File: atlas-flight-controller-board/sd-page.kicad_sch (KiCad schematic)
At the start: 1 part, among them J1 Conn_01x07_Socket

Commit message: finishing up schematic for v1.
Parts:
- J3: renamed from J1; value Conn_01x07_Socket -> XTSD Socket
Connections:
- net +3V3: now reaches J3.2 (Pin_2)
- net GND: now reaches J3.3 (Pin_3)
- net SCK: now reaches J3.4 (Pin_4)
- net MISO: now reaches J3.5 (Pin_5)
- net MOSI: now reaches J3.6 (Pin_6)
- net SD_CS: now reaches J3.7 (Pin_7)
- no-connect marks 0 -> 1

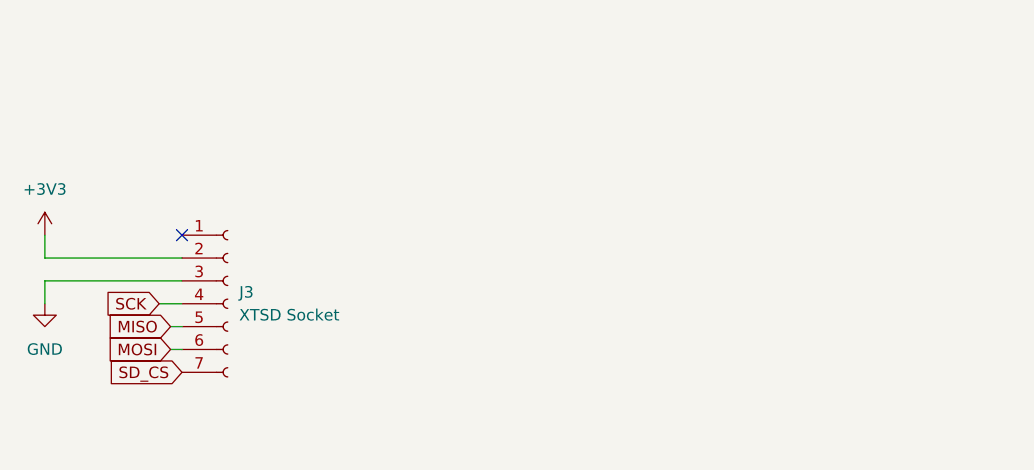
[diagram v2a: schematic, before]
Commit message: removing some olds symbols, adding some new things such as nand flash chip.
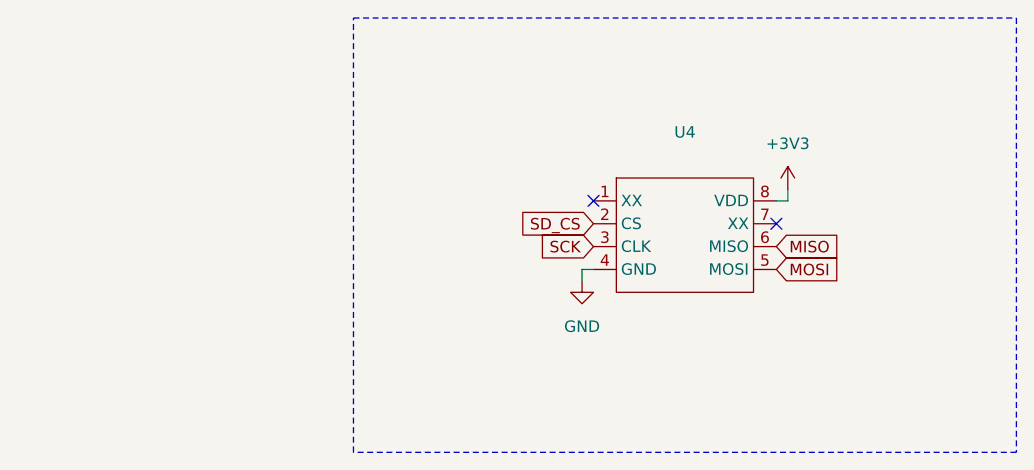
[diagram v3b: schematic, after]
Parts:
- removed J3: XTSD Socket, Connector_PinSocket_2.54mm:PinSocket_1x07_P2.54mm_Vertical, symbol Connector:Conn_01x07_Socket
- added U4: ~, ZDSD16GLGIAG:LGA-8_8x6.2mm_P1.27mm, symbol Interface:ZDSD16GLGIAG
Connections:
- net +3V3: now also U4.8 (VDD)
- net GND: now also U4.4 (GND)
- net MISO: now also U4.6 (MISO)
- net MOSI: now also U4.5 (MOSI)
- net SCK: now also U4.3 (CLK)
- net SD_CS: now also U4.2 (CS)
- no-connect marks 1 -> 2
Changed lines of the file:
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@@
 	(generator_version "9.0")
 	(paper "A4")
+	(rectangle
+		(start 149.86 59.69)
+		(end 223.52 107.95)
+		(stroke
+			(width 0)
+			(type dash)
+		)
+		(fill
+			(type none)
+		)
+	)
 	(no_connect
-		(at 130.81 83.82)
+		(at 196.85 82.55)
+	)
+	(no_connect
+		(at 176.53 80.01)
 	)
 	(wire
 		(pts
-			(xy 115.57 88.9) (xy 115.57 91.44)
+			(xy 175.26 88.9) (xy 175.26 87.63)
 		)
 		(stroke
@@
 	(wire
 		(pts
-			(xy 129.54 96.52) (xy 130.81 96.52)
+			(xy 175.26 87.63) (xy 176.53 87.63)
 		)
 		(stroke
@@
 	(wire
 		(pts
-			(xy 128.27 91.44) (xy 130.81 91.44)
+			(xy 196.85 80.01) (xy 198.12 80.01)
 		)
 		(stroke
@@
 	(wire
 		(pts
-			(xy 129.54 93.98) (xy 130.81 93.98)
-		)
-		(stroke
-			(width 0)
-			(type default)
-		)
-	)
-	(wire
-		(pts
-			(xy 115.57 86.36) (xy 115.57 83.82)
-		)
-		(stroke
-			(width 0)
-			(type default)
-		)
-	)
-	(wire
-		(pts
-			(xy 130.81 86.36) (xy 115.57 86.36)
-		)
-		(stroke
-			(width 0)
-			(type default)
-		)
-	)
-	(wire
-		(pts
-			(xy 130.81 88.9) (xy 115.57 88.9)
+			(xy 198.12 80.01) (xy 198.12 78.74)
 		)
 		(stroke
@@
 	(global_label "MISO"
 		(shape input)
-		(at 129.54 93.98 180)
+		(at 196.85 85.09 0)
 		(fields_autoplaced yes)
 		(effects
@@
 				(size 1.27 1.27)
 			)
-			(justify right)
+			(justify left)
 		)
 		(property "Intersheetrefs" "${INTERSHEET_REFS}"
-			(at 121.9586 93.98 0)
-			(effects
-				(font
-					(size 1.27 1.27)
-				)
-				(justify right)
+			(at 204.4314 85.09 0)
+			(effects
+				(font
+					(size 1.27 1.27)
+				)
+				(justify left)
 				(hide yes)
 			)
@@
 	(global_label "MOSI"
 		(shape input)
-		(at 129.54 96.52 180)
+		(at 196.85 87.63 0)
 		(fields_autoplaced yes)
 		(effects
@@
 				(size 1.27 1.27)
 			)
-			(justify right)
+			(justify left)
 		)
 		(property "Intersheetrefs" "${INTERSHEET_REFS}"
-			(at 121.9586 96.52 0)
-			(effects
-				(font
-					(size 1.27 1.27)
-				)
-				(justify right)
+			(at 204.4314 87.63 0)
+			(effects
+				(font
+					(size 1.27 1.27)
+				)
+				(justify left)
 				(hide yes)
 			)
@@
 	(global_label "SCK"
 		(shape input)
-		(at 128.27 91.44 180)
+		(at 176.53 85.09 180)
 		(fields_autoplaced yes)
 		(effects
@@
 		)
 		(property "Intersheetrefs" "${INTERSHEET_REFS}"
-			(at 121.5353 91.44 0)
+			(at 169.7953 85.09 0)
 			(effects
 				(font
@@
 	(global_label "SD_CS"
 		(shape input)
-		(at 130.81 99.06 180)
+		(at 176.53 82.55 180)
 		(fields_autoplaced yes)
 		(effects
@@
 		)
 		(property "Intersheetrefs" "${INTERSHEET_REFS}"
-			(at 121.8982 99.06 0)
+			(at 167.6182 82.55 0)
 			(effects
 				(font
@@
 	)
 	(symbol
-		(lib_id "power:GND")
-		(at 115.57 91.44 0)
+		(lib_id "power:+3V3")
+		(at 198.12 78.74 0)
 		(unit 1)
 		(exclude_from_sim no)
@@
 		(dnp no)
 		(fields_autoplaced yes)
-		(property "Reference" "#PWR06"
-			(at 115.57 97.79 0)
-			(effects
-				(font
-					(size 1.27 1.27)
-				)
-				(hide yes)
-			)
-		)
-		(property "Value" "GND"
-			(at 115.57 96.52 0)
+		(property "Reference" "#PWR017"
+			(at 198.12 82.55 0)
+			(effects
+				(font
+					(size 1.27 1.27)
+				)
+				(hide yes)
+			)
+		)
+		(property "Value" "+3V3"
+			(at 198.12 73.66 0)
 			(effects
 				(font
@@
 		)
 		(property "Footprint" ""
-			(at 115.57 91.44 0)
+			(at 198.12 78.74 0)
 			(effects
 				(font
@@
 		)
 		(property "Datasheet" ""
-			(at 115.57 91.44 0)
-			(effects
-				(font
-					(size 1.27 1.27)
-				)
-				(hide yes)
-			)
-		)
-		(property "Description" "Power symbol creates a global label with name \"GND\" , ground"
-			(at 115.57 91.44 0)
+			(at 198.12 78.74 0)
+			(effects
+				(font
+					(size 1.27 1.27)
+				)
+				(hide yes)
+			)
+		)
+		(property "Description" "Power symbol creates a global label with name \"+3V3\""
+			(at 198.12 78.74 0)
 			(effects
 				(font
@@
 			(project ""
 				(path "/99efb2d6-b5f7-438c-9ed2-f359400f01a1/0e8824f2-4013-4596-998b-cdfa7c1cf328"
-					(reference "#PWR06")
+					(reference "#PWR017")
 					(unit 1)
 				)
@@
 	)
 	(symbol
-		(lib_id "power:+3V3")
-		(at 115.57 83.82 0)
+		(lib_id "Interface:ZDSD16GLGIAG")
+		(at 186.69 83.82 0)
 		(unit 1)
 		(exclude_from_sim no)
@@
 		(dnp no)
 		(fields_autoplaced yes)
-		(property "Reference" "#PWR05"
-			(at 115.57 87.63 0)
-			(effects
-				(font
-					(size 1.27 1.27)
-				)
-				(hide yes)
-			)
-		)
-		(property "Value" "+3V3"
-			(at 115.57 78.74 0)
-			(effects
-				(font
-					(size 1.27 1.27)
-				)
-			)
-		)
-		(property "Footprint" ""
-			(at 115.57 83.82 0)
+		(property "Reference" "U4"
+			(at 186.69 72.39 0)
+			(effects
+				(font
+					(size 1.27 1.27)
+				)
+			)
+		)
+		(property "Value" "~"
+			(at 186.69 74.93 0)
+			(effects
+				(font
+					(size 1.27 1.27)
+				)
+			)
+		)
+		(property "Footprint" "ZDSD16GLGIAG:LGA-8_8x6.2mm_P1.27mm"
+			(at 186.69 83.82 0)
 			(effects
 				(font
@@
 		)
 		(property "Datasheet" ""
-			(at 115.57 83.82 0)
-			(effects
-				(font
-					(size 1.27 1.27)
-				)
-				(hide yes)
-			)
-		)
-		(property "Description" "Power symbol creates a global label with name \"+3V3\""
-			(at 115.57 83.82 0)
-			(effects
-				(font
-					(size 1.27 1.27)
-				)
-				(hide yes)
-			)
+			(at 186.69 83.82 0)
+			(effects
+				(font
+					(size 1.27 1.27)
+				)
+				(hide yes)
+			)
+		)
+		(property "Description" ""
+			(at 186.69 83.82 0)
+			(effects
+				(font
+					(size 1.27 1.27)
+				)
+				(hide yes)
+			)
+		)
+		(pin "4"
+		)
+		(pin "3"
+		)
+		(pin "2"
 		)
 		(pin "1"
+		)
+		(pin "5"
+		)
+		(pin "7"
+		)
+		(pin "6"
+		)
+		(pin "8"
 		)
 		(instances
 			(project ""
 				(path "/99efb2d6-b5f7-438c-9ed2-f359400f01a1/0e8824f2-4013-4596-998b-cdfa7c1cf328"
-					(reference "#PWR05")
+					(reference "U4")
 					(unit 1)
 				)
@@
 	)
 	(symbol
-		(lib_id "Connector:Conn_01x07_Socket")
-		(at 135.89 91.44 0)
+		(lib_id "power:GND")
+		(at 175.26 88.9 0)
 		(unit 1)
 		(exclude_from_sim no)
@@
 		(dnp no)
 		(fields_autoplaced yes)
-		(property "Reference" "J3"
-			(at 137.16 90.1699 0)
-			(effects
-				(font
-					(size 1.27 1.27)
-				)
-				(justify left)
-			)
-		)
-		(property "Value" "XTSD Socket"
-			(at 137.16 92.7099 0)
-			(effects
-				(font
-					(size 1.27 1.27)
-				)
-				(justify left)
-			)
-		)
-		(property "Footprint" "Connector_PinSocket_2.54mm:PinSocket_1x07_P2.54mm_Vertical"
-			(at 135.89 91.44 0)
-			(effects
-				(font
-					(size 1.27 1.27)
-				)
-				(hide yes)
-			)
-		)
-		(property "Datasheet" "~"
-			(at 135.89 91.44 0)
-			(effects
-				(font
-					(size 1.27 1.27)
-				)
-				(hide yes)
-			)
-		)
-		(property "Description" "Generic connector, single row, 01x07, script generated"
-			(at 135.89 91.44 0)
-			(effects
-				(font
-					(size 1.27 1.27)
-				)
-				(hide yes)
-			)
-		)
-		(pin "3"
-		)
-		(pin "2"
+		(property "Reference" "#PWR018"
+			(at 175.26 95.25 0)
+			(effects
+				(font
+					(size 1.27 1.27)
+				)
+				(hide yes)
+			)
+		)
+		(property "Value" "GND"
+			(at 175.26 93.98 0)
+			(effects
+				(font
+					(size 1.27 1.27)
+				)
+			)
+		)
+		(property "Footprint" ""
+			(at 175.26 88.9 0)
+			(effects
+				(font
+					(size 1.27 1.27)
+				)
+				(hide yes)
+			)
+		)
+		(property "Datasheet" ""
+			(at 175.26 88.9 0)
+			(effects
+				(font
+					(size 1.27 1.27)
+				)
+				(hide yes)
+			)
+		)
+		(property "Description" "Power symbol creates a global label with name \"GND\" , ground"
+			(at 175.26 88.9 0)
+			(effects
+				(font
+					(size 1.27 1.27)
+				)
+				(hide yes)
+			)
 		)
 		(pin "1"
-		)
-		(pin "4"
-		)
-		(pin "6"
-		)
-		(pin "5"
-		)
-		(pin "7"
 		)
 		(instances
 			(project ""
 				(path "/99efb2d6-b5f7-438c-9ed2-f359400f01a1/0e8824f2-4013-4596-998b-cdfa7c1cf328"
-					(reference "J3")
+					(reference "#PWR018")
 					(unit 1)
 				)

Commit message: Bare Schematic (No LEDS, etc added) finished. Begin PCB Layout.
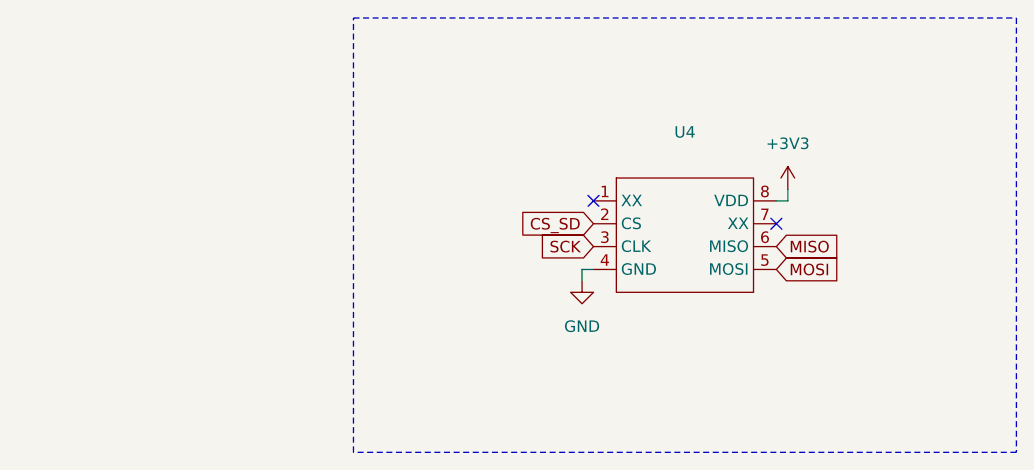
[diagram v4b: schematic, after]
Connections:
- net SD_CS renamed CS_SD
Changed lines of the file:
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@@
 		)
 	)
-	(global_label "SD_CS"
+	(global_label "CS_SD"
 		(shape input)
 		(at 176.53 82.55 180)

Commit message: Sensor and Flash layout finished besides MISO, MOSI resistors (reduce ringing). Added plated M2 mounting holes.
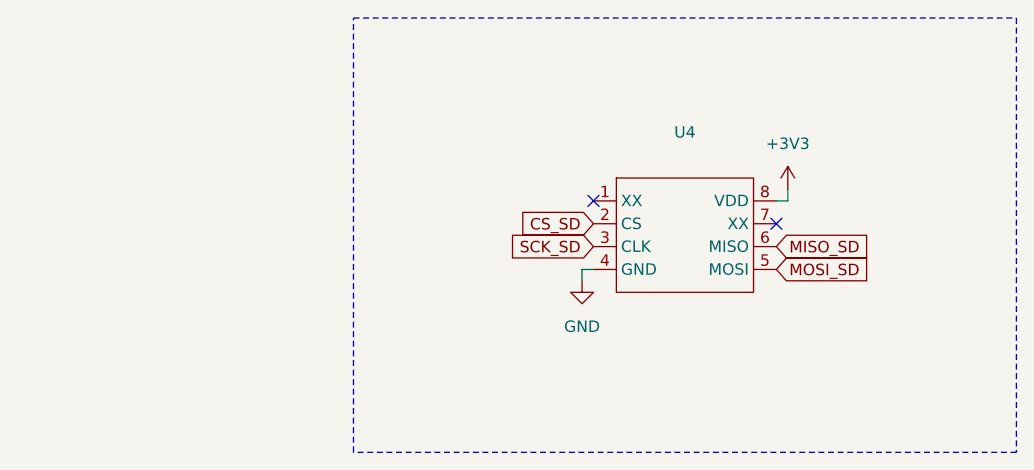
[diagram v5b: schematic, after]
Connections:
- net MISO renamed MISO_SD
- net MOSI renamed MOSI_SD
- net SCK renamed SCK_SD
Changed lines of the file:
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@@
 		)
 	)
-	(global_label "MISO"
+	(global_label "MISO_SD"
 		(shape input)
 		(at 196.85 85.09 0)
@@
 		)
 		(property "Intersheetrefs" "${INTERSHEET_REFS}"
-			(at 204.4314 85.09 0)
+			(at 207.8785 85.09 0)
 			(effects
 				(font
@@
 		)
 	)
-	(global_label "MOSI"
+	(global_label "MOSI_SD"
 		(shape input)
 		(at 196.85 87.63 0)
@@
 		)
 		(property "Intersheetrefs" "${INTERSHEET_REFS}"
-			(at 204.4314 87.63 0)
+			(at 207.8785 87.63 0)
 			(effects
 				(font
@@
 		)
 	)
-	(global_label "SCK"
+	(global_label "SCK_SD"
 		(shape input)
 		(at 176.53 85.09 180)
@@
 		)
 		(property "Intersheetrefs" "${INTERSHEET_REFS}"
-			(at 169.7953 85.09 0)
+			(at 166.3482 85.09 0)
 			(effects
 				(font

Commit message: Done.
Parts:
- removed U4: ~, ZDSD16GLGIAG:LGA-8_8x6.2mm_P1.27mm, symbol Interface:ZDSD16GLGIAG
- added U5: ~, ZDSD16GLGIAG:LGA-8_8x6.2mm_P1.27mm, symbol sd-nand-flash:ZDSD16GLGIAG
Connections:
- net +3V3: now also U5.8 (VDD)
- net CS_SD: now also U5.2 (CS)
- net GND: now also U5.4 (GND)
- net MISO_SD: now also U5.6 (MISO)
- net MOSI_SD: now also U5.5 (MOSI)
- net SCK_SD: now also U5.3 (CLK)
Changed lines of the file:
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@@
+	)
+	(no_connect
+		(at 176.53 80.01)
 	)
 	(no_connect
 		(at 196.85 82.55)
 	)
-	(no_connect
-		(at 176.53 80.01)
+	(wire
+		(pts
+			(xy 196.85 80.01) (xy 198.12 80.01)
+		)
+		(stroke
+			(width 0)
+			(type default)
+		)
 	)
 	(wire
@@
 	(wire
 		(pts
-			(xy 196.85 80.01) (xy 198.12 80.01)
+			(xy 198.12 80.01) (xy 198.12 78.74)
 		)
 		(stroke
@@
 		)
 	)
-	(wire
-		(pts
-			(xy 198.12 80.01) (xy 198.12 78.74)
-		)
-		(stroke
-			(width 0)
-			(type default)
-		)
-	)
 	(global_label "MISO_SD"
 		(shape input)
@@
 		)
 	)
+	(global_label "CS_SD"
+		(shape input)
+		(at 176.53 82.55 180)
+		(fields_autoplaced yes)
+		(effects
+			(font
+				(size 1.27 1.27)
+			)
+			(justify right)
+		)
+		(property "Intersheetrefs" "${INTERSHEET_REFS}"
+			(at 167.6182 82.55 0)
+			(effects
+				(font
+					(size 1.27 1.27)
+				)
+				(justify right)
+				(hide yes)
+			)
+		)
+	)
 	(global_label "MOSI_SD"
 		(shape input)
@@
 		)
 	)
-	(global_label "CS_SD"
-		(shape input)
-		(at 176.53 82.55 180)
-		(fields_autoplaced yes)
-		(effects
-			(font
-				(size 1.27 1.27)
-			)
-			(justify right)
-		)
-		(property "Intersheetrefs" "${INTERSHEET_REFS}"
-			(at 167.6182 82.55 0)
-			(effects
-				(font
-					(size 1.27 1.27)
-				)
-				(justify right)
-				(hide yes)
+	(symbol
+		(lib_id "sd-nand-flash:ZDSD16GLGIAG")
+		(at 186.69 83.82 0)
+		(unit 1)
+		(exclude_from_sim no)
+		(in_bom yes)
+		(on_board yes)
+		(dnp no)
+		(fields_autoplaced yes)
+		(property "Reference" "U5"
+			(at 186.69 72.39 0)
+			(effects
+				(font
+					(size 1.27 1.27)
+				)
+			)
+		)
+		(property "Value" "~"
+			(at 186.69 74.93 0)
+			(effects
+				(font
+					(size 1.27 1.27)
+				)
+			)
+		)
+		(property "Footprint" "ZDSD16GLGIAG:LGA-8_8x6.2mm_P1.27mm"
+			(at 186.69 83.82 0)
+			(effects
+				(font
+					(size 1.27 1.27)
+				)
+				(hide yes)
+			)
+		)
+		(property "Datasheet" "https://www.lcsc.com/datasheet/C19727141.pdf?spm=wm.sxq.inf.ggs&lcsc_vid=R1hXUwcEFgQLBgBXElNcVgcEFFdfUFJTRVReBV0CRVgxVlNRRFhZU1FeQFZZUjsOAxUeFF5JWBYZEEoBGA4JCwFIFA4DSA%3D%3D"
+			(at 186.69 83.82 0)
+			(effects
+				(font
+					(size 1.27 1.27)
+				)
+				(hide yes)
+			)
+		)
+		(property "Description" "16 Gbit Nand Flashchip with SPI and SD interface."
+			(at 186.69 83.82 0)
+			(effects
+				(font
+					(size 1.27 1.27)
+				)
+				(hide yes)
+			)
+		)
+		(pin "4"
+		)
+		(pin "8"
+		)
+		(pin "3"
+		)
+		(pin "2"
+		)
+		(pin "5"
+		)
+		(pin "7"
+		)
+		(pin "6"
+		)
+		(pin "1"
+		)
+		(instances
+			(project ""
+				(path "/99efb2d6-b5f7-438c-9ed2-f359400f01a1/0e8824f2-4013-4596-998b-cdfa7c1cf328"
+					(reference "U5")
+					(unit 1)
+				)
+			)
+		)
+	)
+	(symbol
+		(lib_id "power:GND")
+		(at 175.26 88.9 0)
+		(unit 1)
+		(exclude_from_sim no)
+		(in_bom yes)
+		(on_board yes)
+		(dnp no)
+		(fields_autoplaced yes)
+		(property "Reference" "#PWR03"
+			(at 175.26 95.25 0)
+			(effects
+				(font
+					(size 1.27 1.27)
+				)
+				(hide yes)
+			)
+		)
+		(property "Value" "GND"
+			(at 175.26 93.98 0)
+			(effects
+				(font
+					(size 1.27 1.27)
+				)
+			)
+		)
+		(property "Footprint" ""
+			(at 175.26 88.9 0)
+			(effects
+				(font
+					(size 1.27 1.27)
+				)
+				(hide yes)
+			)
+		)
+		(property "Datasheet" ""
+			(at 175.26 88.9 0)
+			(effects
+				(font
+					(size 1.27 1.27)
+				)
+				(hide yes)
+			)
+		)
+		(property "Description" "Power symbol creates a global label with name \"GND\" , ground"
+			(at 175.26 88.9 0)
+			(effects
+				(font
+					(size 1.27 1.27)
+				)
+				(hide yes)
+			)
+		)
+		(pin "1"
+		)
+		(instances
+			(project "atlas-flight-controller-board"
+				(path "/99efb2d6-b5f7-438c-9ed2-f359400f01a1/0e8824f2-4013-4596-998b-cdfa7c1cf328"
+					(reference "#PWR03")
+					(unit 1)
+				)
 			)
 		)
@@
 		(dnp no)
 		(fields_autoplaced yes)
-		(property "Reference" "#PWR017"
+		(property "Reference" "#PWR04"
 			(at 198.12 82.55 0)
 			(effects
@@
 		)
 		(instances
-			(project ""
+			(project "atlas-flight-controller-board"
 				(path "/99efb2d6-b5f7-438c-9ed2-f359400f01a1/0e8824f2-4013-4596-998b-cdfa7c1cf328"
-					(reference "#PWR017")
+					(reference "#PWR04")
 					(unit 1)
 				)
-			)
-		)
-	)
-	(symbol
-		(lib_id "Interface:ZDSD16GLGIAG")
-		(at 186.69 83.82 0)
-		(unit 1)
-		(exclude_from_sim no)
-		(in_bom yes)
-		(on_board yes)
-		(dnp no)
-		(fields_autoplaced yes)
-		(property "Reference" "U4"
-			(at 186.69 72.39 0)
-			(effects
-				(font
-					(size 1.27 1.27)
-				)
-			)
-		)
-		(property "Value" "~"
-			(at 186.69 74.93 0)
-			(effects
-				(font
-					(size 1.27 1.27)
-				)
-			)
-		)
-		(property "Footprint" "ZDSD16GLGIAG:LGA-8_8x6.2mm_P1.27mm"
-			(at 186.69 83.82 0)
-			(effects
-				(font
-					(size 1.27 1.27)
-				)
-				(hide yes)
-			)
-		)
-		(property "Datasheet" ""
-			(at 186.69 83.82 0)
-			(effects
-				(font
-					(size 1.27 1.27)
-				)
-				(hide yes)
-			)
-		)
-		(property "Description" ""
-			(at 186.69 83.82 0)
-			(effects
-				(font
-					(size 1.27 1.27)
-				)
-				(hide yes)
-			)
-		)
-		(pin "4"
-		)
-		(pin "3"
-		)
-		(pin "2"
-		)
-		(pin "1"
-		)
-		(pin "5"
-		)
-		(pin "7"
-		)
-		(pin "6"
-		)
-		(pin "8"
-		)
-		(instances
-			(project ""
-				(path "/99efb2d6-b5f7-438c-9ed2-f359400f01a1/0e8824f2-4013-4596-998b-cdfa7c1cf328"
-					(reference "U4")
-					(unit 1)
-				)
-			)
-		)
-	)
-	(symbol
-		(lib_id "power:GND")
-		(at 175.26 88.9 0)
-		(unit 1)
-		(exclude_from_sim no)
-		(in_bom yes)
-		(on_board yes)
-		(dnp no)
-		(fields_autoplaced yes)
-		(property "Reference" "#PWR018"
-			(at 175.26 95.25 0)
-			(effects
-				(font
-					(size 1.27 1.27)
-				)
-				(hide yes)
-			)
-		)
-		(property "Value" "GND"
-			(at 175.26 93.98 0)
-			(effects
-				(font
-					(size 1.27 1.27)
-				)
-			)
-		)
-		(property "Footprint" ""
-			(at 175.26 88.9 0)
-			(effects
-				(font
-					(size 1.27 1.27)
-				)
-				(hide yes)
-			)
-		)
-		(property "Datasheet" ""
-			(at 175.26 88.9 0)
-			(effects
-				(font
-					(size 1.27 1.27)
-				)
-				(hide yes)
-			)
-		)
-		(property "Description" "Power symbol creates a global label with name \"GND\" , ground"
-			(at 175.26 88.9 0)
-			(effects
-				(font
-					(size 1.27 1.27)
-				)
-				(hide yes)
-			)
-		)
-		(pin "1"
-		)
-		(instances
-			(project ""
-				(path "/99efb2d6-b5f7-438c-9ed2-f359400f01a1/0e8824f2-4013-4596-998b-cdfa7c1cf328"
-					(reference "#PWR018")
-					(unit 1)
-				)
